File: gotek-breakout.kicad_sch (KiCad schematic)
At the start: 5 parts, among them J1 FFC 10x1 0.5mm, J2 USB_A, J3 OLED, J4 Encoder

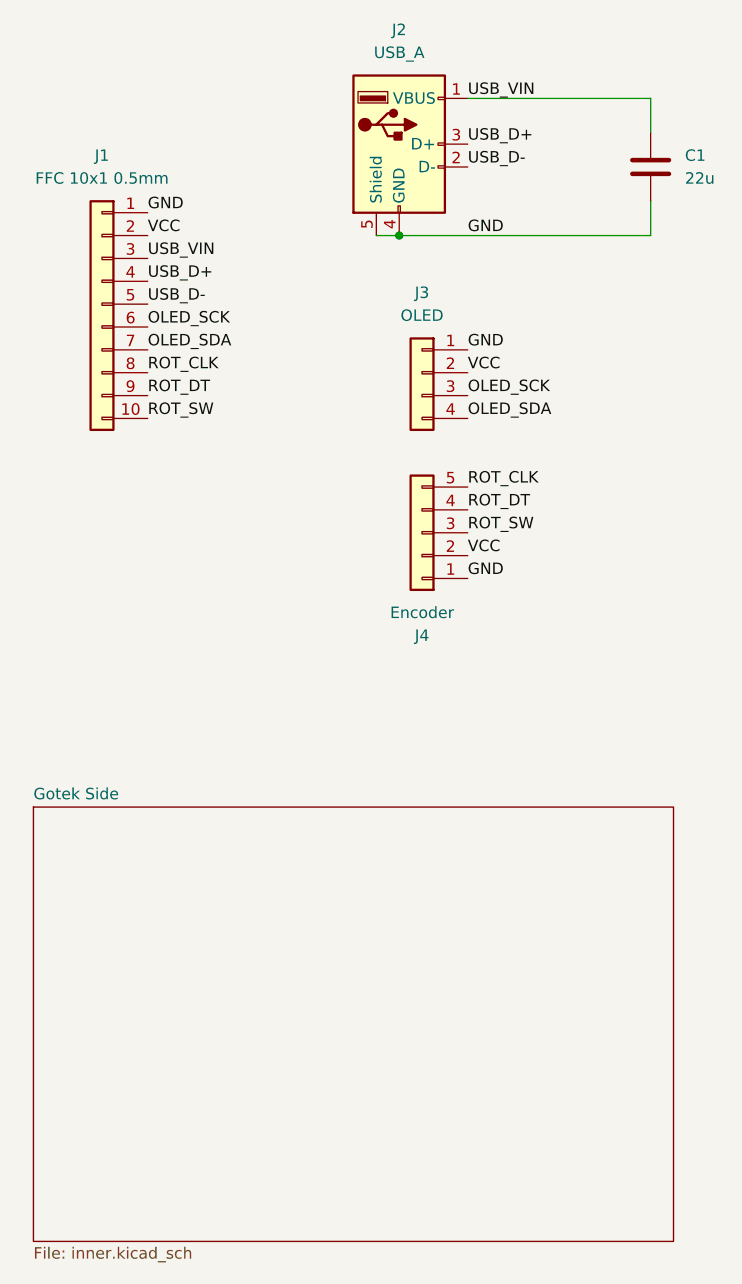
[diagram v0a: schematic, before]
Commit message: Breakout board only for newer goteks
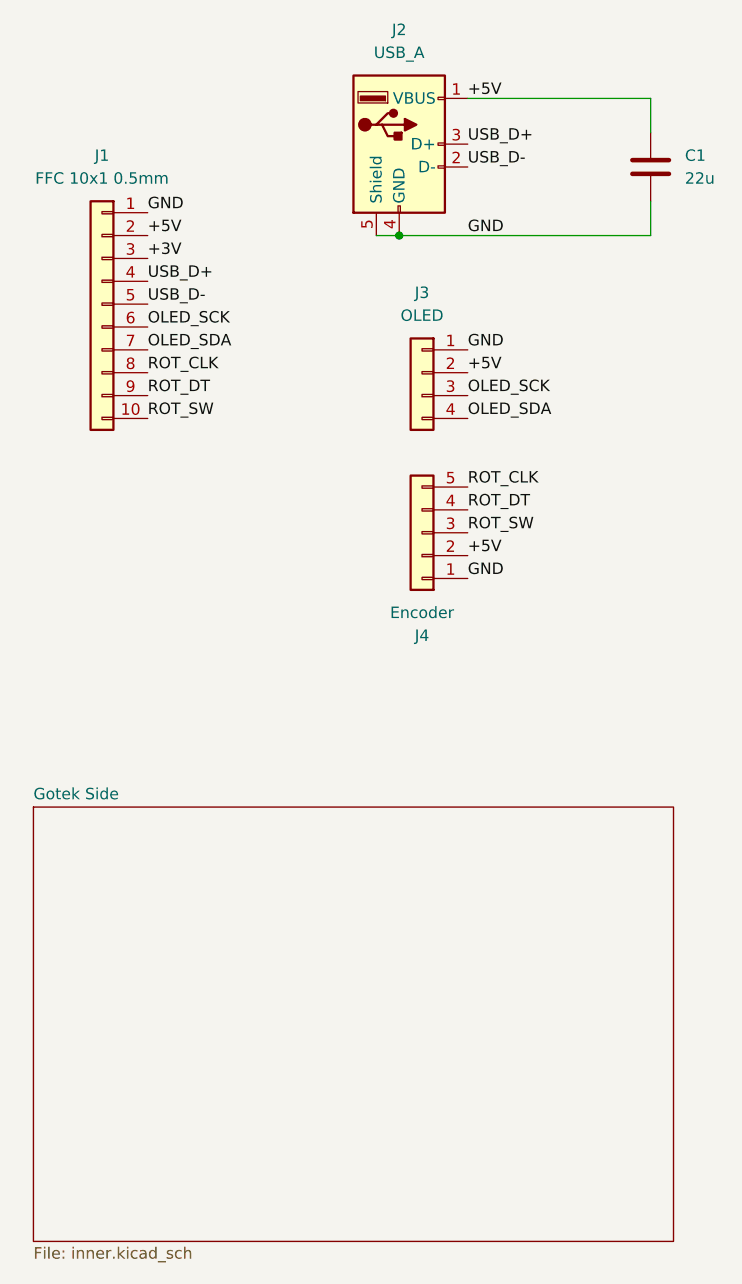
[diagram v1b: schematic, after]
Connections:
- net VCC is gone; now on net +5V: J1.2 (Pin_2), J3.2 (Pin_2), J4.2 (Pin_2)
- net USB_VIN renamed +5V
- net +5V: no longer J1.3 (Pin_3)
- new net +3V: J1.3 (Pin_3)
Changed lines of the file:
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@@
 		)
 	)
-	(label "USB_VIN"
+	(label "+5V"
 		(at 73.66 43.18 0)
 		(fields_autoplaced yes)
@@
 		)
 	)
-	(label "USB_VIN"
-		(at 38.1 60.96 0)
-		(fields_autoplaced yes)
-		(effects
-			(font
-				(size 1.27 1.27)
-			)
-			(justify left bottom)
-		)
-	)
 	(label "OLED_SCK"
 		(at 73.66 76.2 0)
@@
 		)
 	)
-	(label "VCC"
+	(label "+5V"
 		(at 73.66 73.66 0)
 		(fields_autoplaced yes)
@@
 	(label "ROT_SW"
 		(at 38.1 78.74 0)
+		(fields_autoplaced yes)
+		(effects
+			(font
+				(size 1.27 1.27)
+			)
+			(justify left bottom)
+		)
+	)
+	(label "+3V"
+		(at 38.1 60.96 0)
 		(fields_autoplaced yes)
 		(effects
@@
 		)
 	)
-	(label "VCC"
+	(label "+5V"
 		(at 73.66 93.98 0)
 		(fields_autoplaced yes)
@@
 		)
 	)
-	(label "VCC"
+	(label "+5V"
 		(at 38.1 58.42 0)
 		(fields_autoplaced yes)
